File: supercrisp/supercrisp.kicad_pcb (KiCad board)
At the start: 2 copper layers, 140 x 91 mm, 144 parts, among them J1 SWD, J2 AudioJack4, J3 SWD, J4 AudioJack4, SW1 SW_SPDT, SW10 SW_Push, SW11 SW_Push, SW12 SW_Push, SW13 SW_Push, SW14 SW_Push, SW15 SW_Push, SW16 SW_Push, SW17 SW_Push, SW18 SW_Push, SW19 SW_Push, SW2 SW_Push, SW20 SW_Push, SW21 SW_Push, SW22 SW_Push, SW23 SW_Push, SW24 SW_Push, SW25 SW_Push, SW26 SW_Push, SW27 SW_Push, SW28 SW_SPDT, SW3 SW_Push, SW4 SW_Push, SW5 SW_Push, SW6 SW_Push, SW7 SW_Push, SW8 SW_Push, SW9 SW_Push, U1 TPS82140

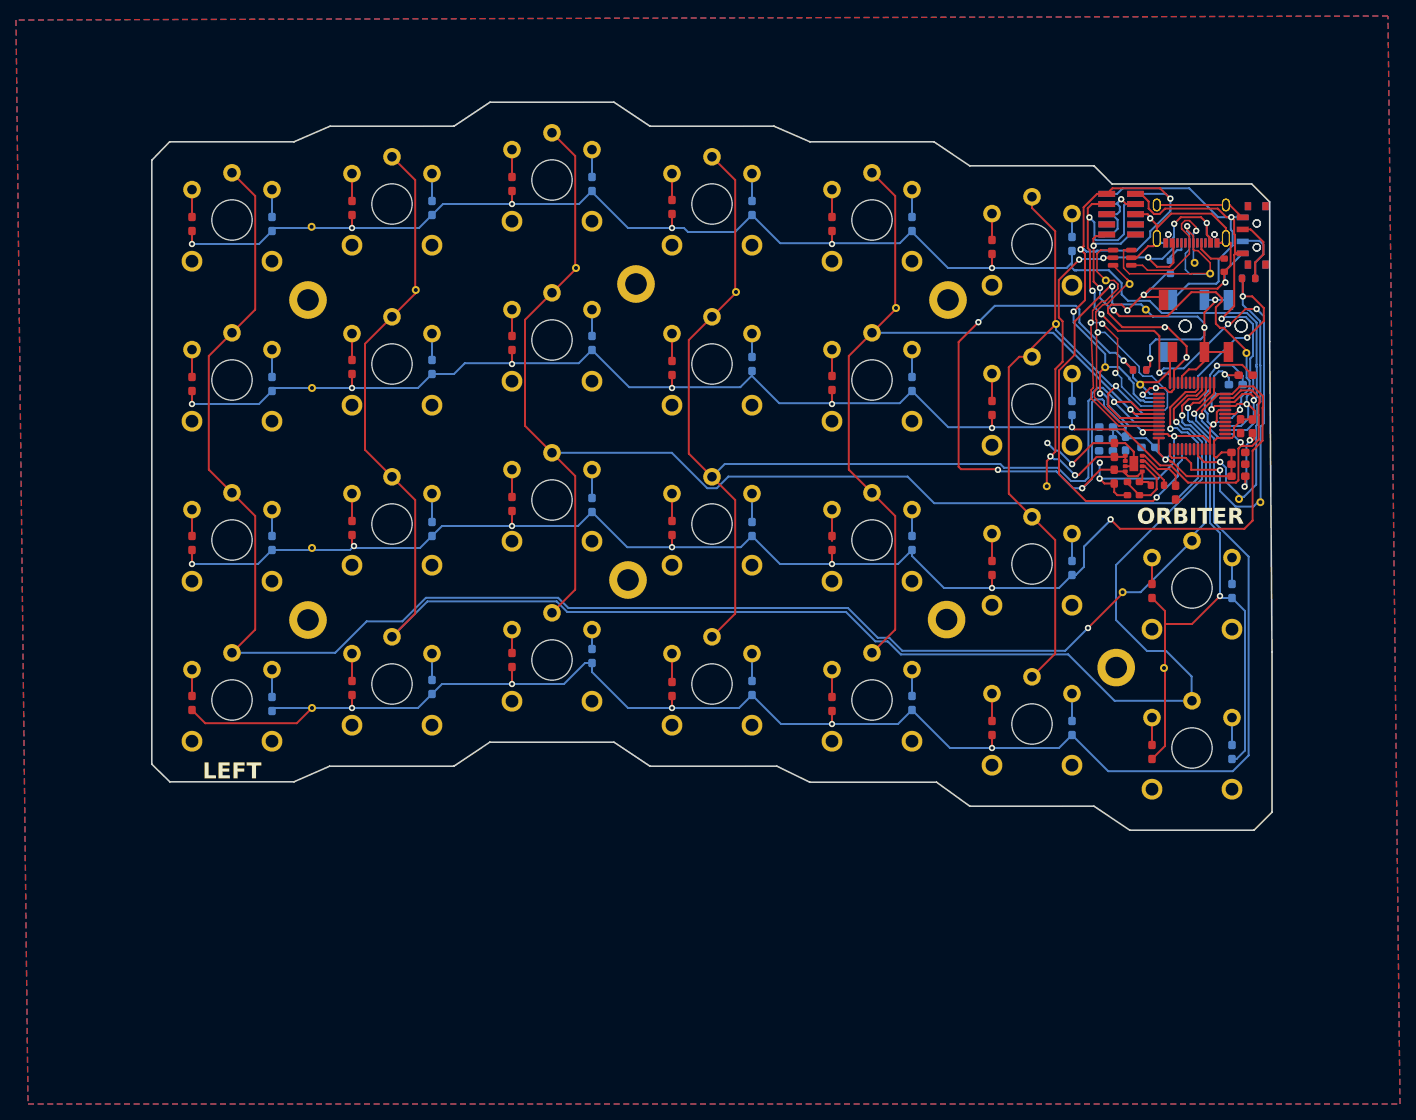
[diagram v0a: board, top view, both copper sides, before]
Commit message: GND copper fill zone now aligned with edge cut
Move USB port closer to edge
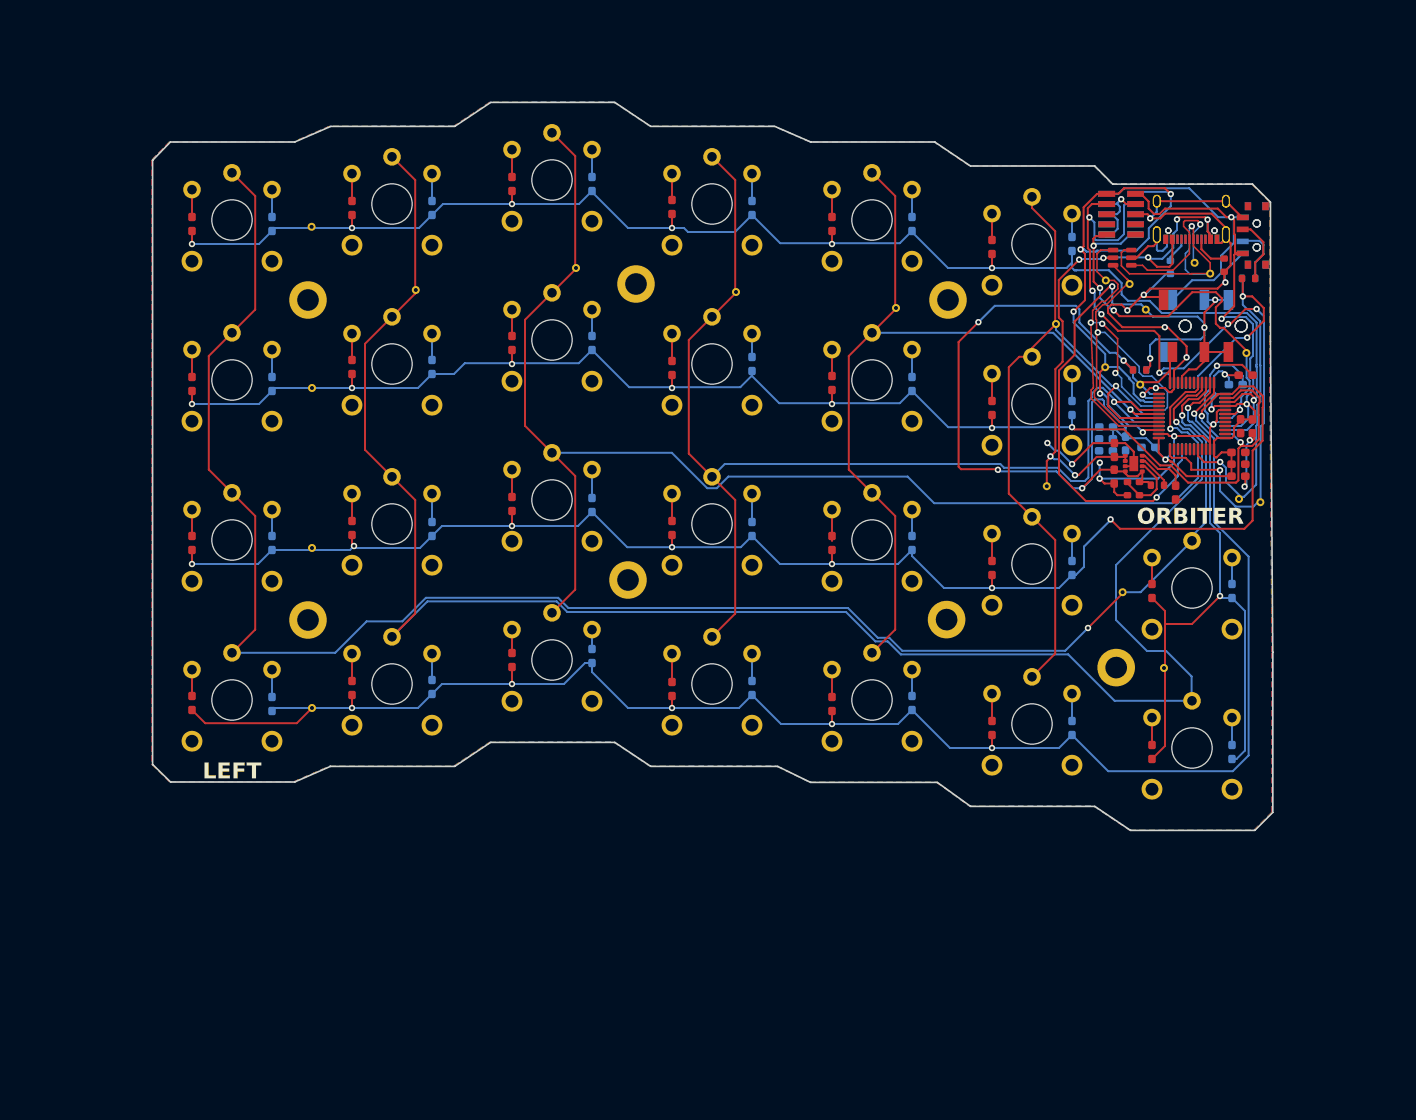
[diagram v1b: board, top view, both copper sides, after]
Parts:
- moved USB_P1 0.48 mm to (199.9, 43.7)
- moved USB_P2 0.47 mm to (199.9, 43.7)
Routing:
- net /VBUS: track 77.2 -> 79.1 mm
- net /USB_CONN_DP: track 31.3 -> 30.5 mm
- net /USB_CONN_DN: track 19.4 -> 20.1 mm

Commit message: Add via stitching around edge
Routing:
- net GND: vias 18 -> 173
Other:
- board text removed: "TODO add via stitching"

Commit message: Add JLCPCB hide text in silk
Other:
- board text added: "JLCJLCJLCJLC"
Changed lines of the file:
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@@
 		(allow_soldermask_bridges_in_footprints no)
 		(pcbplotparams
-			(layerselection 0x0009000_7ffffffe)
+			(layerselection 0x000d033_ffffffff)
 			(plot_on_all_layers_selection 0x0000000_00000000)
 			(disableapertmacros no)
@@
 			(dashed_line_gap_ratio 3.000000)
 			(svgprecision 4)
-			(plotframeref no)
+			(plotframeref yes)
 			(viasonmask no)
 			(mode 1)
@@
 			(sketchpadsonfab no)
 			(subtractmaskfromsilk no)
-			(outputformat 3)
+			(outputformat 1)
 			(mirror no)
 			(drillshape 0)
@@
 		)
 	)
+	(gr_text "JLCJLCJLCJLC"
+		(at 197.85 69.580642 0)
+		(layer "F.SilkS")
+		(effects
+			(font
+				(size 0.4 0.4)
+				(thickness 0.1)
+				(bold yes)
+			)
+			(justify left bottom)
+		)
+	)
